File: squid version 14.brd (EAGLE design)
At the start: 33 x 61 mm, 62 parts, among them J2 ATMEL_PROGRAMMER_HEADERNL, U2 MCP73832

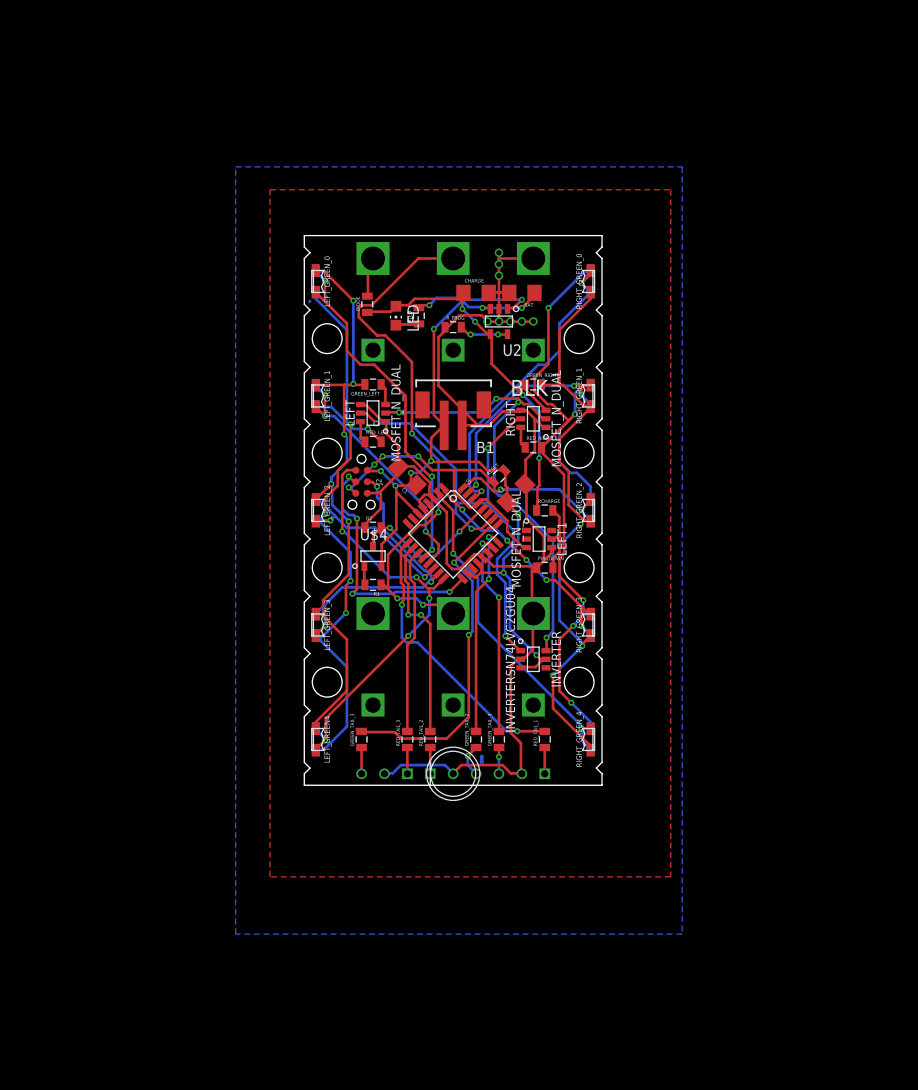
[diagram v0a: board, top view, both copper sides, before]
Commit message: added some comments
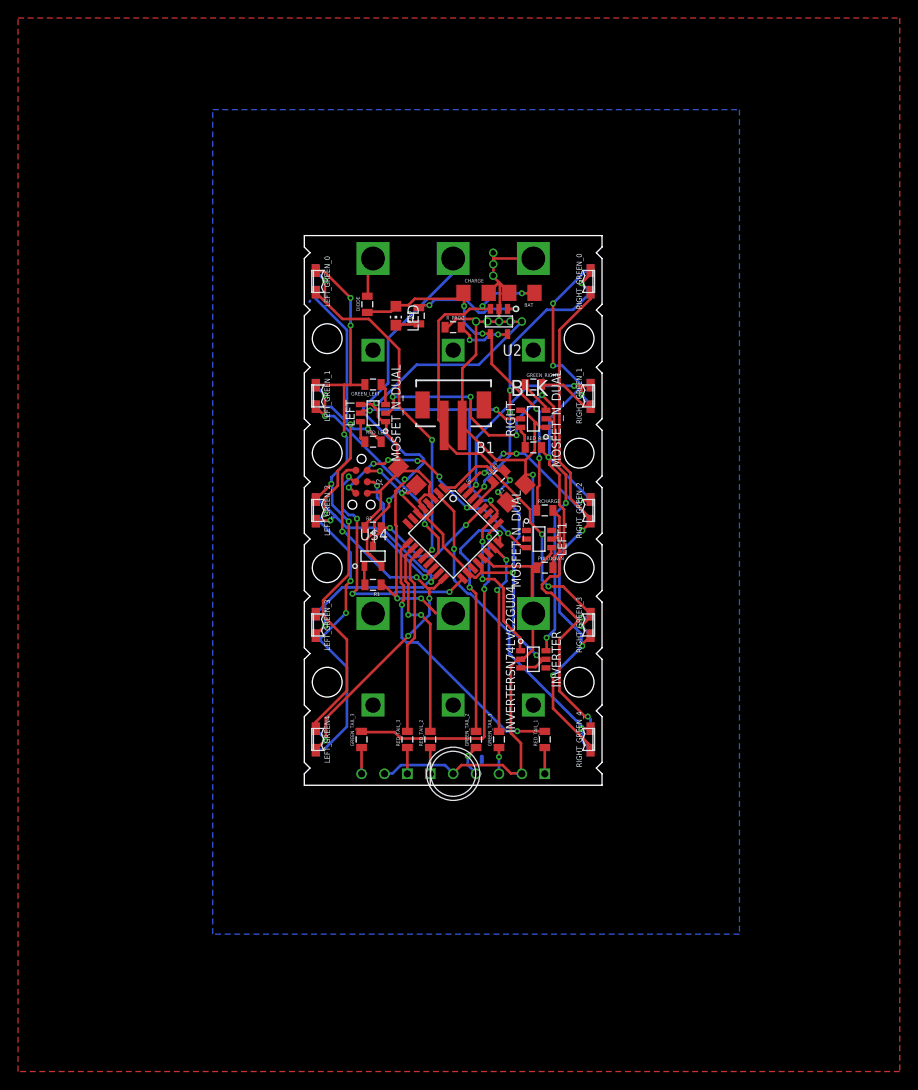
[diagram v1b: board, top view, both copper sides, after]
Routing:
- net GND: track 157.4 -> 172.8 mm, vias 8 -> 10
- net N$7: track 57.4 -> 50.1 mm, vias 4 -> 5
- net N$12: track 80.1 -> 73.7 mm
- net PD3: track 26.0 -> 31.1 mm, vias 5 -> 3
- net N$2: track 51.9 -> 56.3 mm, vias 4 -> 6
- net VBAT: track 98.7 -> 102.9 mm, vias 10 -> 9
- net PC1: track 23.5 -> 27.4 mm
- net N$9: track 60.3 -> 56.4 mm, vias 4 -> 3
- net RESET: track 34.1 -> 30.8 mm, vias 4 -> 7
- net PD2: track 18.5 -> 20.9 mm, vias 2 -> 4
- net PC0: track 23.0 -> 21.6 mm
- net STAT: track 14.0 -> 12.7 mm
- net N$21: track 39.9 -> 40.8 mm
- net N$15: track 5.49 -> 6.29 mm
- net N$11: track 66.5 -> 67.3 mm
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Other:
- board text added: "Jul 30 2014"
- board text removed: "May 30 2014"

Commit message: disconnect top center tube holder
Does not need an electrical connection
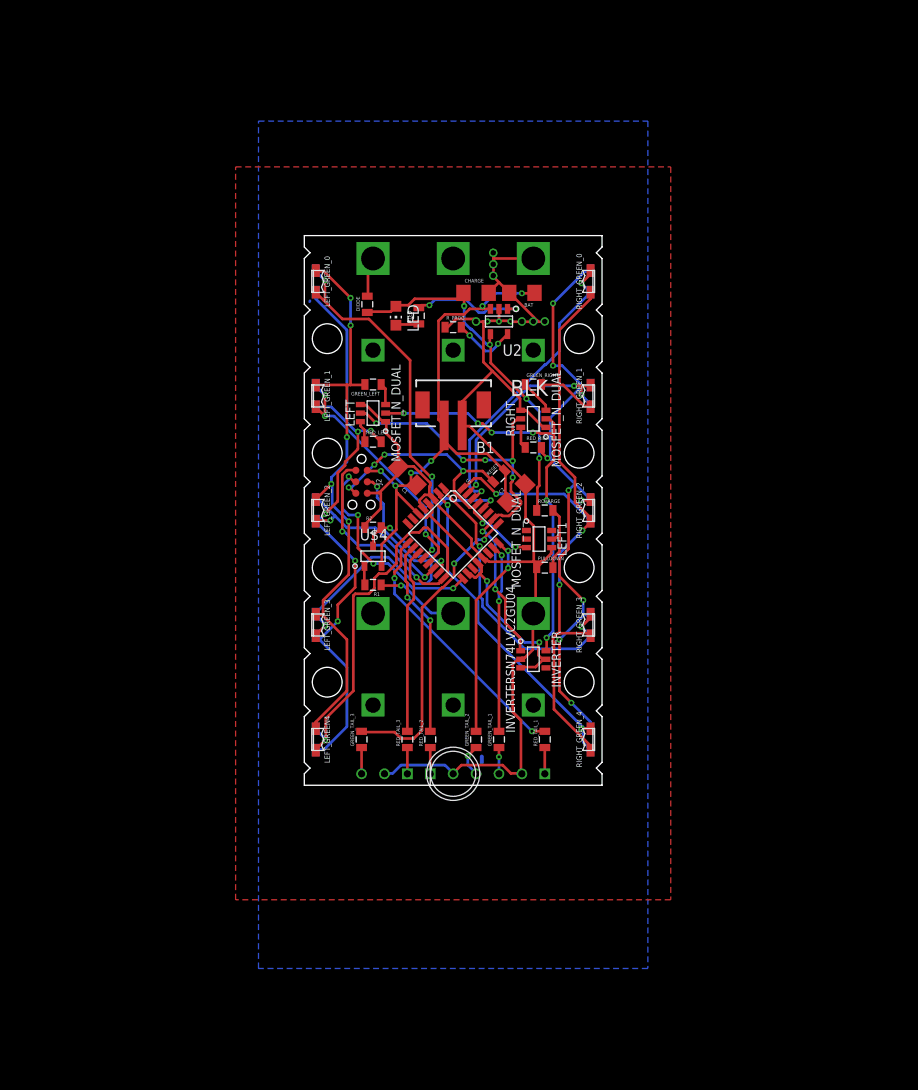
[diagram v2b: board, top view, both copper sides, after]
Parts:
- renumbered CENTER_BOTTOM to SENSOR_T, CENTER_TOP to SENSOR_B
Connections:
- net N$9: no longer SENSOR_T.1
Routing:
- net N$9: track 56.4 -> 9.34 mm, vias 3 -> 1
- net PB4: track 47.2 -> 62.3 mm, vias 5 -> 3
- net GND: track 172.8 -> 158.9 mm
- net N$2: track 56.3 -> 46.9 mm
- net N$12: track 73.7 -> 68.0 mm, vias 5 -> 7
- net N$4: track 17.3 -> 22.9 mm
- net VBAT: track 102.9 -> 97.7 mm, vias 9 -> 8
- net PC1: track 27.4 -> 22.9 mm
- net PB3: track 34.0 -> 38.0 mm
- net PC2: track 38.3 -> 34.3 mm
- net PB5: track 28.5 -> 24.5 mm
- net RESET: track 30.8 -> 34.3 mm, vias 7 -> 6
- net PD2: track 20.9 -> 18.6 mm, vias 4 -> 2
- net PD5: track 31.2 -> 29.3 mm
- net PD3: track 31.1 -> 32.7 mm, vias 3 -> 2
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
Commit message: assign values of ballast resistors
Put proper values of ballast resistors into schematic
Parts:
- GREEN_TAIL_1, GREEN_TAIL_2, GREEN_TAIL_3: value 100 -> 43
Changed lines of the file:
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@@
 <element name="CENTER" library="ERIC" package="LED_KINGBRIGHT_BICOLOR_INDICATOR_LAMP" value="LED_RED_GREEN_CC" x="17.78" y="1.27" rot="R90"/>
 <element name="U$13" library="ERIC" package="LED_KINGBRIGHT_BICOLOR_INDICATOR_LAMP" value="LED_RED_GREEN_CC" x="10.16" y="1.27" rot="MR90"/>
-<element name="GREEN_TAIL_1" library="SparkFun-Passives" package="0805" value="100" x="22.86" y="5.08" rot="R90"/>
-<element name="GREEN_TAIL_2" library="SparkFun-Passives" package="0805" value="100" x="20.32" y="5.08" rot="R90"/>
-<element name="GREEN_TAIL_3" library="SparkFun-Passives" package="0805" value="100" x="7.62" y="5.08" rot="R90"/>
+<element name="GREEN_TAIL_1" library="SparkFun-Passives" package="0805" value="43" x="22.86" y="5.08" rot="R90"/>
+<element name="GREEN_TAIL_2" library="SparkFun-Passives" package="0805" value="43" x="20.32" y="5.08" rot="R90"/>
+<element name="GREEN_TAIL_3" library="SparkFun-Passives" package="0805" value="43" x="7.62" y="5.08" rot="R90"/>
 <element name="RED_TAIL_1" library="SparkFun-Passives" package="0805" value="100" x="27.94" y="5.08" rot="R90"/>
 <element name="RED_TAIL_2" library="SparkFun-Passives" package="0805" value="100" x="15.24" y="5.08" rot="R90"/>

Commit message: correct current programming resistor value
Major mistake in current programming resistor!! Changed from 24 to
4.7K!!!
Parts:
- GREEN_TAIL_1, GREEN_TAIL_2, GREEN_TAIL_3: value 43 -> 45
- R_PROG: value 25 -> 4.7K
- renumbered LEFT1 to CHARGING, U$10 to GND_BOT, U$17 to GND_TOP, U$8 to CHARGE_TOP
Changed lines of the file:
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@@
 <element name="CHARGE" library="SparkFun" package="1206" value="4.7u" x="20.32" y="54.61"/>
 <element name="BAT" library="SparkFun" package="1206" value="4.7u" x="25.4" y="54.61" rot="R180"/>
-<element name="R_PROG" library="SparkFun" package="0805" value="25" x="17.78" y="50.8"/>
+<element name="R_PROG" library="SparkFun" package="0805" value="4.7K" x="17.78" y="50.8"/>
 <element name="LED" library="led" package="CHIP-LED0805" value="RED" x="11.43" y="52.07" rot="R180"/>
 <element name="RLED" library="SparkFun" package="0805" value="300" x="13.97" y="52.07" rot="R90"/>
@@
 <attribute name="NAME" x="20.32" y="36.83" size="1.27" layer="25"/>
 </element>
-<element name="U$8" library="Keystone" package="HORIZONTAL_QUICK_CONNECT_3547" value="FEMALE_QUICK_FIT_TERMINAL" x="8.89" y="53.34" rot="MR0"/>
-<element name="U$10" library="Keystone" package="HORIZONTAL_QUICK_CONNECT_3547" value="FEMALE_QUICK_FIT_TERMINAL" x="26.67" y="53.34" rot="MR0"/>
+<element name="CHARGE_TOP" library="Keystone" package="HORIZONTAL_QUICK_CONNECT_3547" value="FEMALE_QUICK_FIT_TERMINAL" x="8.89" y="53.34" rot="MR0"/>
+<element name="GND_BOT" library="Keystone" package="HORIZONTAL_QUICK_CONNECT_3547" value="FEMALE_QUICK_FIT_TERMINAL" x="26.67" y="53.34" rot="MR0"/>
 <element name="U2" library="ERIC" package="SOT-23(OT)5_LEAD" value="MCP73832" x="22.86" y="51.435" rot="R180"/>
 <element name="C2" library="SparkFun" package="1206" value="4.7u" x="24.765" y="32.385" rot="R45"/>
@@
 <element name="R2" library="SparkFun" package="0805" value="30K" x="8.89" y="28.575"/>
 <element name="CHARGE_BOTTOM" library="Keystone" package="HORIZONTAL_QUICK_CONNECT_3547" value="FEMALE_QUICK_FIT_TERMINAL" x="8.89" y="13.97" rot="MR0"/>
-<element name="U$17" library="Keystone" package="HORIZONTAL_QUICK_CONNECT_3547" value="FEMALE_QUICK_FIT_TERMINAL" x="26.67" y="13.97" rot="MR0"/>
-<element name="LEFT1" library="ERIC" package="SOT-23-6" value="MOSFET_N_DUAL" x="27.305" y="27.305" rot="R270"/>
+<element name="GND_TOP" library="Keystone" package="HORIZONTAL_QUICK_CONNECT_3547" value="FEMALE_QUICK_FIT_TERMINAL" x="26.67" y="13.97" rot="MR0"/>
+<element name="CHARGING" library="ERIC" package="SOT-23-6" value="MOSFET_N_DUAL" x="27.305" y="27.305" rot="R270"/>
 <element name="RCHARGE" library="SparkFun" package="0805" value="300" x="27.94" y="30.48"/>
 <element name="PULLDOWN" library="SparkFun" package="0805" value="10K" x="27.94" y="24.13"/>
@@
 <element name="CENTER" library="ERIC" package="LED_KINGBRIGHT_BICOLOR_INDICATOR_LAMP" value="LED_RED_GREEN_CC" x="17.78" y="1.27" rot="R90"/>
 <element name="U$13" library="ERIC" package="LED_KINGBRIGHT_BICOLOR_INDICATOR_LAMP" value="LED_RED_GREEN_CC" x="10.16" y="1.27" rot="MR90"/>
-<element name="GREEN_TAIL_1" library="SparkFun-Passives" package="0805" value="43" x="22.86" y="5.08" rot="R90"/>
-<element name="GREEN_TAIL_2" library="SparkFun-Passives" package="0805" value="43" x="20.32" y="5.08" rot="R90"/>
-<element name="GREEN_TAIL_3" library="SparkFun-Passives" package="0805" value="43" x="7.62" y="5.08" rot="R90"/>
+<element name="GREEN_TAIL_1" library="SparkFun-Passives" package="0805" value="45" x="22.86" y="5.08" rot="R90"/>
+<element name="GREEN_TAIL_2" library="SparkFun-Passives" package="0805" value="45" x="20.32" y="5.08" rot="R90"/>
+<element name="GREEN_TAIL_3" library="SparkFun-Passives" package="0805" value="45" x="7.62" y="5.08" rot="R90"/>
 <element name="RED_TAIL_1" library="SparkFun-Passives" package="0805" value="100" x="27.94" y="5.08" rot="R90"/>
 <element name="RED_TAIL_2" library="SparkFun-Passives" package="0805" value="100" x="15.24" y="5.08" rot="R90"/>
@@
 <contactref element="RIGHT" pad="4"/>
 <contactref element="RIGHT" pad="1"/>
-<contactref element="U$10" pad="1"/>
+<contactref element="GND_BOT" pad="1"/>
 <contactref element="INVERTER" pad="2"/>
 <contactref element="R2" pad="1"/>
-<contactref element="U$17" pad="1"/>
-<contactref element="LEFT1" pad="4"/>
+<contactref element="GND_TOP" pad="1"/>
+<contactref element="CHARGING" pad="4"/>
 <contactref element="PULLDOWN" pad="1"/>
 <contactref element="U$7" pad="2"/>
@@
 <signal name="RESET">
 <contactref element="J2" pad="5"/>
-<contactref element="LEFT1" pad="3"/>
+<contactref element="CHARGING" pad="3"/>
 <contactref element="RESET" pad="1"/>
 <contactref element="U1" pad="29"/>
@@
 </signal>
 <signal name="VCHARGE">
-<contactref element="U$8" pad="1"/>
+<contactref element="CHARGE_TOP" pad="1"/>
 <contactref element="DIODE" pad="2"/>
 <wire x1="8.3312" y1="57.912" x2="8.3312" y2="54.2544" width="0.3" layer="1"/>
@@
 </signal>
 <signal name="N$3">
-<contactref element="LEFT1" pad="5"/>
+<contactref element="CHARGING" pad="5"/>
 <contactref element="RCHARGE" pad="2"/>
 <contactref element="PULLDOWN" pad="2"/>
